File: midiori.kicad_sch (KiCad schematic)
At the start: 73 parts, among them J1 midiori-rescue_x68000_expansi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, J2 Conn_ARM_JTAG_SWD_10, J3 AudioJack3, J4 Mini-DIN-5, J5 AudioJack3, J6 AudioJack3, U1 74LCX07, U10 ICE40HX1K-VQ100, U11 AP2205K-3.3, U12 AK4432, U13 TL074, U14 AP2205K-3.3, U2 AT25SF081-SSHD-X, U3 AP2127K-1.2, U4 SN74LVC8T245DWR, U5 SN74LVC8T245DWR, U6 SN74LVC8T245DWR, U7 SN74LVC8T245DWR, U8 SN74LVC8T245DWR, U9 SN74LVC8T245DWR, X1 16MHz, X2 24.576MHz

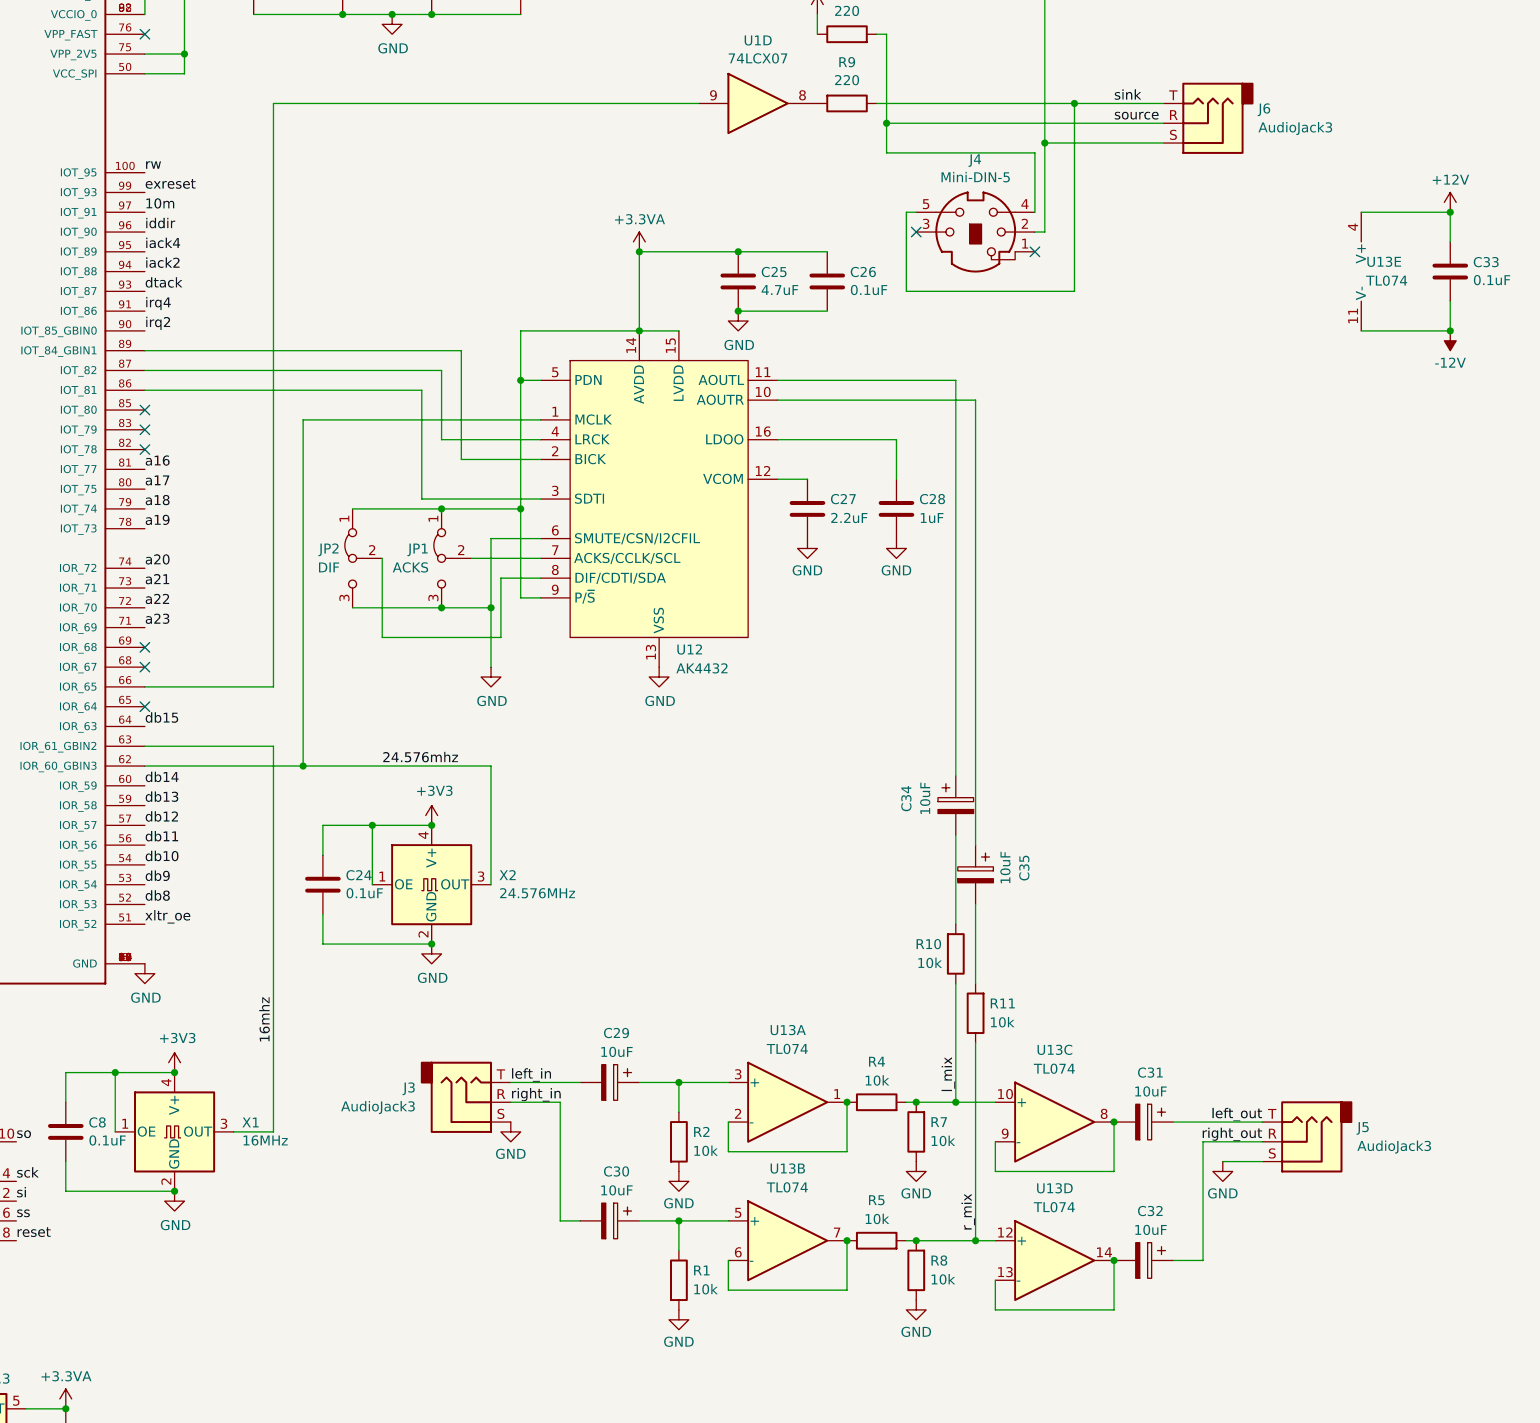
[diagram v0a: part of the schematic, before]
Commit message: small schematic changes
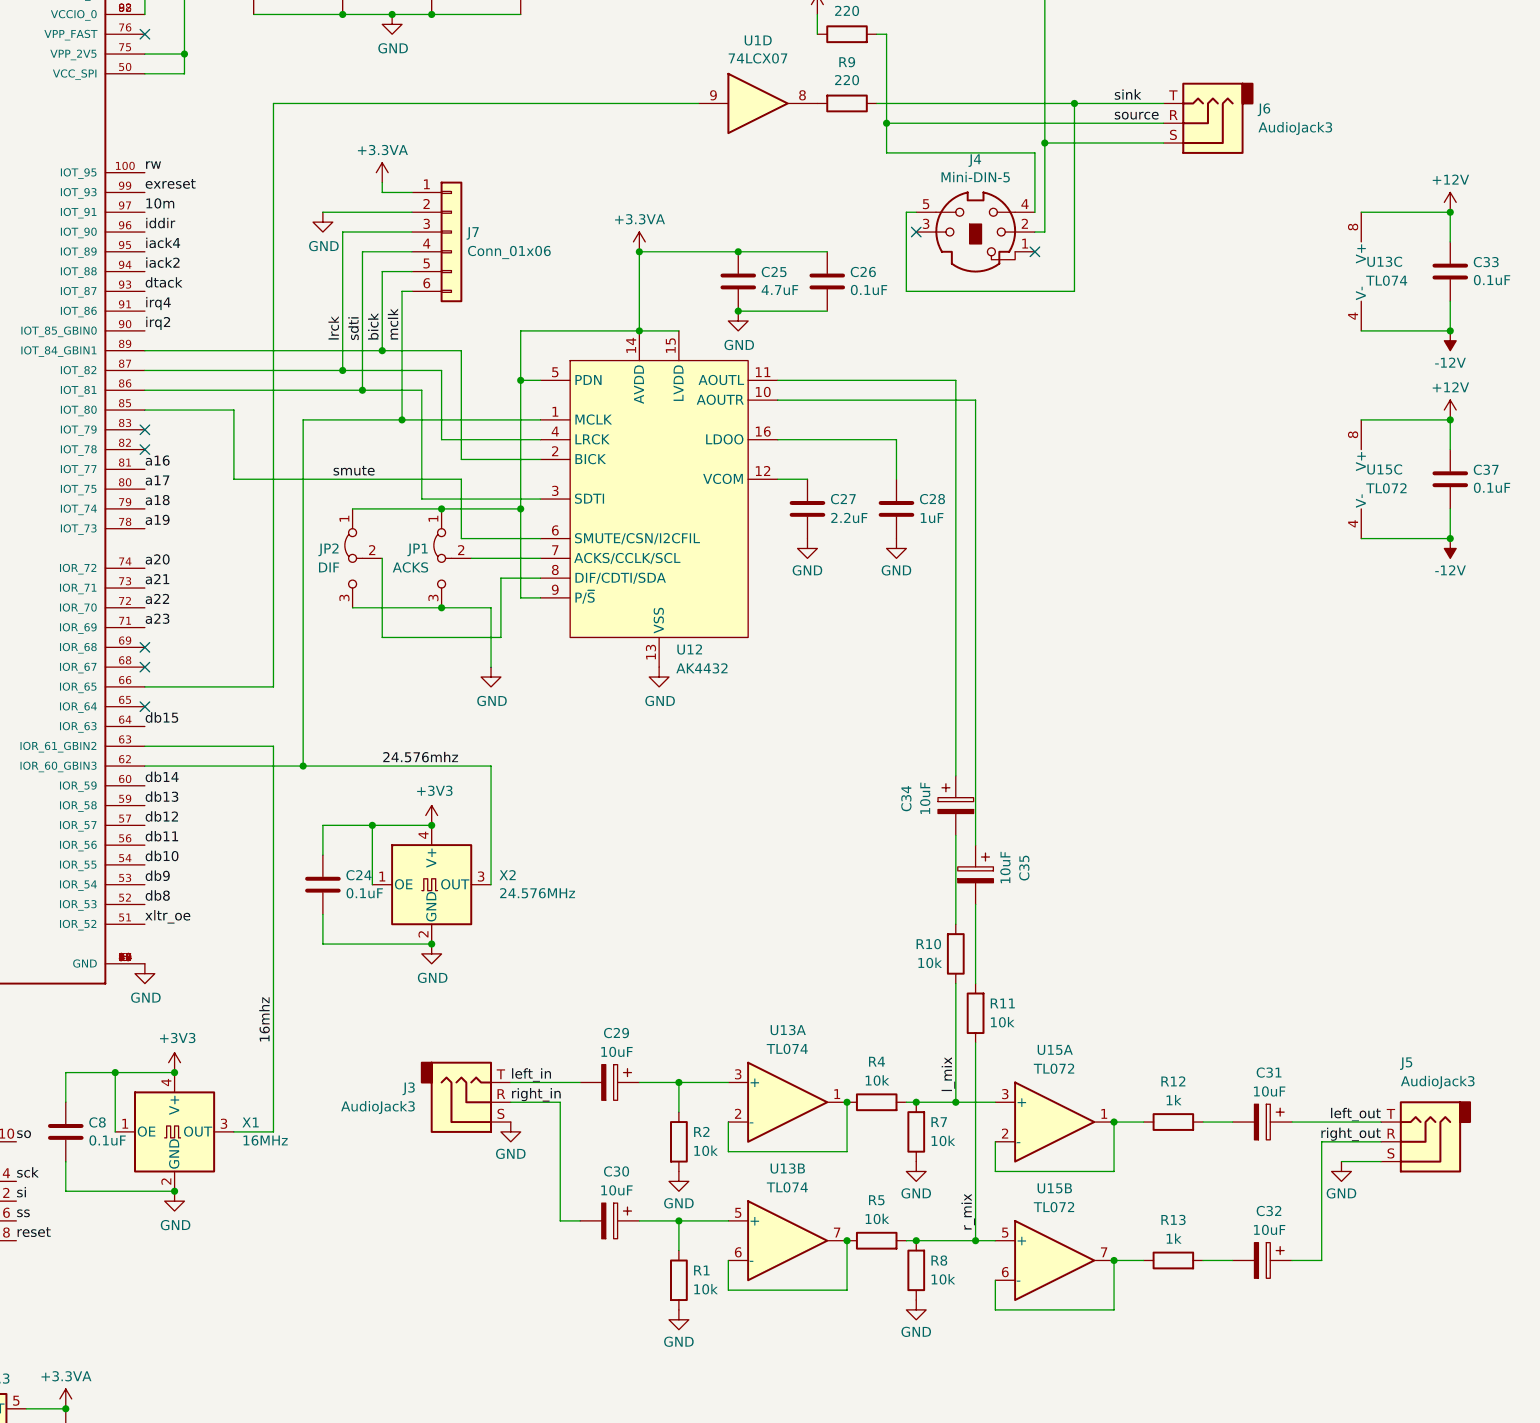
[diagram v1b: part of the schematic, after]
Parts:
- removed unit 4 of U13
- removed unit 5 of U13
- added C37: 0.1uF, Capacitor_SMD:C_0805_2012Metric, symbol Device:C
- added J7: Conn_01x06, Connector_PinHeader_2.54mm:PinHeader_1x06_P2.54mm_Vertical, symbol Connector_Generic:Conn_01x06
- added R12, R13: 1k, Resistor_SMD:R_0805_2012Metric, symbol Device:R
- added U15: TL072, Package_SO:SOIC-8_3.9x4.9mm_P1.27mm, symbol Amplifier_Operational:TL072
- C24, C8: footprint Capacitor_SMD:C_0805_2012Metric_Pad1.15x1.40mm_HandSolder -> Capacitor_SMD:C_0805_2012Metric
- C27, C28: footprint (none) -> Capacitor_SMD:C_0805_2012Metric
- C29, C30, C31, C32, C34, C35: footprint (none) -> Capacitor_SMD:C_Elec_5x5.8; Digikey (none) -> 565-HHXD350ARA220ME61GCT-ND
- J3, J5, J6: footprint (none) -> Connector_Audio:Jack_3.5mm_CUI_SJ1-3533NG_Horizontal
- R1, R10, R11, R2, R4, R5, R7, R8: footprint (none) -> Resistor_SMD:R_0805_2012Metric
- U10: Digikey (none) -> 220-1567-ND
- U12: Digikey (none) -> 974-1078-1-ND
- U13: footprint (none) -> Package_SO:SOIC-8_3.9x4.9mm_P1.27mm; symbol Amplifier_Operational:TL074 -> Amplifier_Operational:TL072
- U4, U5, U6, U7, U8, U9: Digikey (none) -> 1727-8095-1-ND
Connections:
- net +12V: now also U13.8 (V+), C37.1, U15.8 (V+)
- net +3.3VA: now also J7.1 (Pin_1)
- net -12V: now also U13.4 (V-), C37.2, U15.4 (V-)
- net 24.576mhz: now also J7.6 (Pin_6)
- net GND: now also J7.2 (Pin_2); no longer U12.6 (SMUTE/CSN/I2CFIL)
- net l_mix: now also U15.3 (+); no longer U13.10 (+)
- net r_mix: now also U15.5 (+)
- net smute: now reaches U10.85 (IOT_80)
- net smute: now also U12.6 (SMUTE/CSN/I2CFIL)
- net sdti: now reaches U10.86 (IOT_81), U12.3 (SDTI)
- net sdti: now also J7.4 (Pin_4)
- net lrck: now reaches U10.87 (IOT_82), U12.4 (LRCK)
- net lrck: now also J7.3 (Pin_3)
- net bick: now reaches U10.89 (IOT_84_GBIN1), U12.2 (BICK)
- net bick: now also J7.5 (Pin_5)
- net at C32.2: now also R13.2
- new net: R12.1, U15.1, U15.2 (-)
- new net: C31.2, R12.2
- new net: R13.1, U15.6 (-), U15.7
- no-connect marks 50 -> 49
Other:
- moved on the sheet: C31, C32, J5

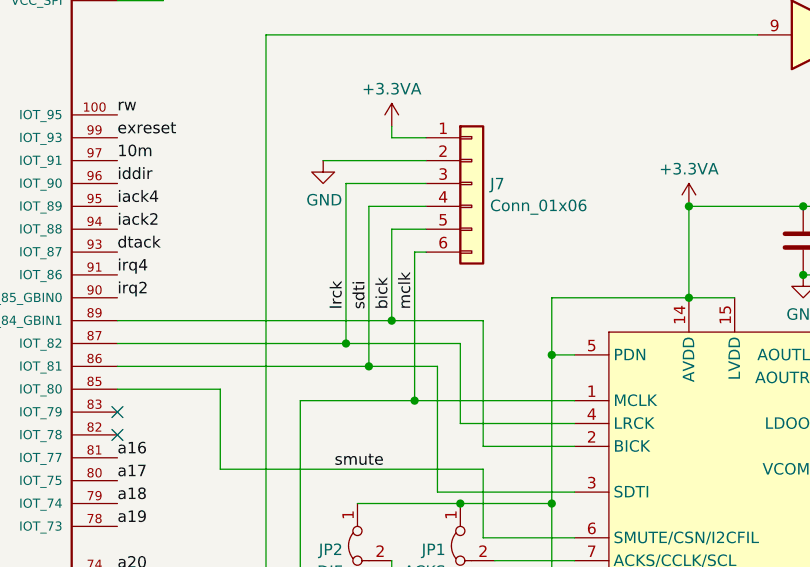
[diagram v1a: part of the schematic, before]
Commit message: convert pcb version
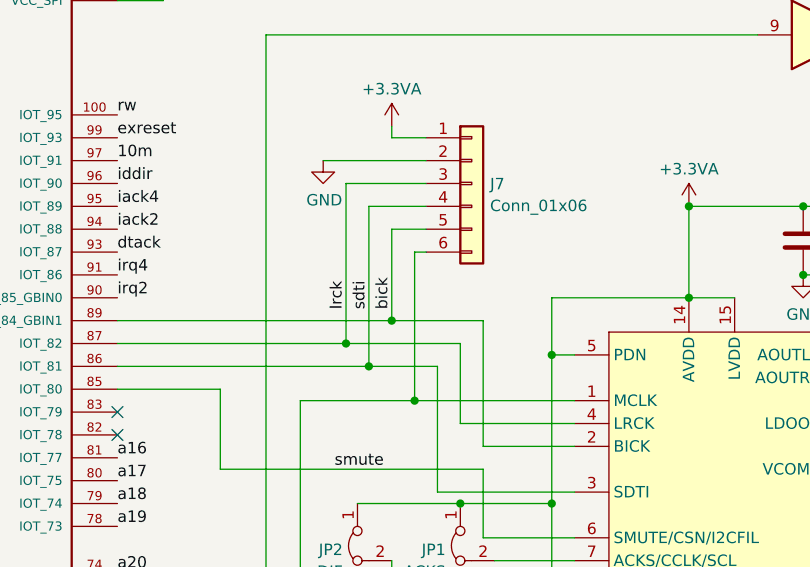
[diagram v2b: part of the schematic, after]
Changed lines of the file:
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@@
-		)
-	)
-	(label "mclk"
-		(at 278.13 102.87 90)
-		(fields_autoplaced yes)
-		(effects
-			(font
-				(size 1.27 1.27)
-			)
-			(justify left bottom)
 		)
 	)

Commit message: switch to single psu translator
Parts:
- added R14: R, symbol Device:R
- U4, U5, U6, U7, U8, U9: value SN74LVC8T245DWR -> SN74LVC245APW; footprint SOIC127P1030X265-24N -> Package_SO:TSSOP-20_4.4x6.5mm_P0.65mm; symbol midiori-rescue:SN74LVC8T245DWR-SN74LVC8T245DWR-midiori-rescue-midiori-rescue -> Logic_LevelTranslator:SN74LVC245APW
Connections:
- net +3V3: now also U4.20 (VCC), U5.20 (VCC), U6.20 (VCC), U7.20 (VCC), U8.1 (DIR), U8.20 (VCC), U9.20 (VCC), R14.1; no longer U4.23 (VCCB), U4.24 (VCCB), U5.23 (VCCB), U5.24 (VCCB), U6.23 (VCCB), U6.24 (VCCB), U7.23 (VCCB), U7.24 (VCCB), U8.23 (VCCB), U8.24 (VCCB), U9.23 (VCCB), U9.24 (VCCB)
- net +5V: no longer U4.1 (VCCA), U4.2 (DIR), U5.1 (VCCA), U5.2 (DIR), U6.1 (VCCA), U6.2 (DIR), U7.1 (VCCA), U8.1 (VCCA), U8.2 (DIR), U9.1 (VCCA)
- net 10MHz: now also U8.2 (A1); no longer U8.3 (A1)
- net 10m: now also U8.18 (B1); no longer U8.21 (B1)
- net AB1: now also U4.9 (A8); no longer U4.10 (A8)
- net AB10: now also U5.7 (A6); no longer U5.8 (A6)
- net AB11: now also U5.6 (A5); no longer U5.7 (A5)
- net AB12: now also U5.5 (A4); no longer U5.6 (A4)
- net AB13: now also U5.4 (A3); no longer U5.5 (A3)
- net AB14: now also U5.3 (A2); no longer U5.4 (A2)
- net AB15: now also U5.2 (A1); no longer U5.3 (A1)
- net AB16: now also U6.9 (A8); no longer U6.10 (A8)
- net AB17: now also U6.8 (A7); no longer U6.9 (A7)
- net AB18: now also U6.7 (A6); no longer U6.8 (A6)
- net AB19: now also U6.6 (A5); no longer U6.7 (A5)
- net AB2: now also U4.8 (A7); no longer U4.9 (A7)
- net AB20: now also U6.5 (A4); no longer U6.6 (A4)
- net AB21: now also U6.4 (A3); no longer U6.5 (A3)
- net AB22: now also U6.3 (A2); no longer U6.4 (A2)
- net AB23: now also U6.2 (A1); no longer U6.3 (A1)
- net AB3: now also U4.7 (A6); no longer U4.8 (A6)
- net AB4: now also U4.6 (A5); no longer U4.7 (A5)
- net AB5: now also U4.5 (A4); no longer U4.6 (A4)
- net AB6: now also U4.4 (A3); no longer U4.5 (A3)
- net AB7: now also U4.3 (A2); no longer U4.4 (A2)
- net AB8: now also U5.9 (A8); no longer U5.10 (A8)
- net AB9: now also U5.8 (A7); no longer U5.9 (A7)
- net AS: now also U8.6 (A5); no longer U8.7 (A5)
- net DB0: now also U7.9 (A8); no longer U7.10 (A8)
- net DB1: now also U7.8 (A7); no longer U7.9 (A7)
- net DB10: now also U9.7 (A6); no longer U9.8 (A6)
- net DB11: now also U9.6 (A5); no longer U9.7 (A5)
- net DB12: now also U9.5 (A4); no longer U9.6 (A4)
- net DB13: now also U9.4 (A3); no longer U9.5 (A3)
- net DB14: now also U9.3 (A2); no longer U9.4 (A2)
- net DB15: now also U9.2 (A1); no longer U9.3 (A1)
- net DB2: now also U7.7 (A6); no longer U7.8 (A6)
- net DB3: now also U7.6 (A5); no longer U7.7 (A5)
- net DB4: now also U7.5 (A4); no longer U7.6 (A4)
- net DB5: now also U7.4 (A3); no longer U7.5 (A3)
- net DB6: now also U7.3 (A2); no longer U7.4 (A2)
- net DB7: now also U7.2 (A1); no longer U7.3 (A1)
- net DB8: now also U9.9 (A8); no longer U9.10 (A8)
- net DB9: now also U9.8 (A7); no longer U9.9 (A7)
- net EXRESET: now also U8.3 (A2); no longer U8.4 (A2)
- net GND: now also U4.10 (GND), U4.18 (B1), U4.19 (~{OE}), U4.2 (A1), U5.10 (GND), U5.19 (~{OE}), U6.10 (GND), U6.19 (~{OE}), U7.10 (GND), U8.10 (GND), U8.19 (~{OE}), U9.10 (GND); no longer U4.11 (GND), U4.12 (GND), U4.13 (GND), U4.21 (B1), U4.22 (OE), U4.3 (A1), U5.11 (GND), U5.12 (GND), U5.13 (GND), U5.22 (OE), U6.11 (GND), U6.12 (GND), U6.13 (GND), U6.22 (OE), U7.11 (GND), U7.12 (GND), U7.13 (GND), U8.11 (GND), U8.12 (GND), U8.13 (GND), U8.22 (OE), U9.11 (GND), U9.12 (GND), U9.13 (GND)
- net IACK2: now also U8.7 (A6); no longer U8.8 (A6)
- net IACK4: now also U8.8 (A7); no longer U8.9 (A7)
- net IDDIR: now also U7.1 (DIR), U8.9 (A8), U9.1 (DIR); no longer U7.2 (DIR), U8.10 (A8), U9.2 (DIR)
- net LDS: now also U8.5 (A4); no longer U8.6 (A4)
- net RW: now also U8.4 (A3); no longer U8.5 (A3)
- net a1: now also U4.11 (B8); no longer U4.14 (B8)
- net a16: now also U6.11 (B8); no longer U6.14 (B8)
- net a17: now also U6.12 (B7); no longer U6.15 (B7)
- net a18: now also U6.13 (B6); no longer U6.16 (B6)
- net a19: now also U6.14 (B5); no longer U6.17 (B5)
- net a2: now also U4.12 (B7); no longer U4.15 (B7)
- net a20: now also U6.15 (B4); no longer U6.18 (B4)
- net a21: now also U6.16 (B3); no longer U6.19 (B3)
- net a22: now also U6.17 (B2); no longer U6.20 (B2)
- net a23: now also U6.18 (B1); no longer U6.21 (B1)
- net a3: now also U4.13 (B6); no longer U4.16 (B6)
- net a4: now also U4.14 (B5); no longer U4.17 (B5)
- net a5: now also U4.15 (B4); no longer U4.18 (B4)
- net a6: now also U4.16 (B3); no longer U4.19 (B3)
- net a7: now also U4.17 (B2); no longer U4.20 (B2)
- net ab10: now also U5.13 (B6); no longer U5.16 (B6)
- net ab11: now also U5.14 (B5); no longer U5.17 (B5)
- net ab12: now also U5.15 (B4); no longer U5.18 (B4)
- net ab13: now also U5.16 (B3); no longer U5.19 (B3)
- net ab14: now also U5.17 (B2); no longer U5.20 (B2)
- net ab15: now also U5.18 (B1); no longer U5.21 (B1)
- net ab8: now also U5.11 (B8); no longer U5.14 (B8)
- net ab9: now also U5.12 (B7); no longer U5.15 (B7)
- net as: now also U8.14 (B5); no longer U8.17 (B5)
- net d0: now also U7.11 (B8); no longer U7.14 (B8)
- net d1: now also U7.12 (B7); no longer U7.15 (B7)
- net d2: now also U7.13 (B6); no longer U7.16 (B6)
- net d3: now also U7.14 (B5); no longer U7.17 (B5)
- net d4: now also U7.15 (B4); no longer U7.18 (B4)
- net d5: now also U7.16 (B3); no longer U7.19 (B3)
- net d6: now also U7.17 (B2); no longer U7.20 (B2)
- net d7: now also U7.18 (B1); no longer U7.21 (B1)
- net db10: now also U9.13 (B6); no longer U9.16 (B6)
- net db11: now also U9.14 (B5); no longer U9.17 (B5)
- net db12: now also U9.15 (B4); no longer U9.18 (B4)
- net db13: now also U9.16 (B3); no longer U9.19 (B3)
- net db14: now also U9.17 (B2); no longer U9.20 (B2)
- net db15: now also U9.18 (B1); no longer U9.21 (B1)
- net db8: now also U9.11 (B8); no longer U9.14 (B8)
- net db9: now also U9.12 (B7); no longer U9.15 (B7)
- net exreset: now also U8.17 (B2); no longer U8.20 (B2)
- net iack2: now also U8.13 (B6); no longer U8.16 (B6)
- net iack4: now also U8.12 (B7); no longer U8.15 (B7)
- net iddir: now also U8.11 (B8); no longer U8.14 (B8)
- net lds: now also U8.15 (B4); no longer U8.18 (B4)
- net rw: now also U8.16 (B3); no longer U8.19 (B3)
- net xltr_oe: now also U7.19 (~{OE}), U9.19 (~{OE}); no longer U7.22 (OE), U9.22 (OE)
- net addr_dir: now reaches U10.69 (IOR_68)
- net addr_dir: now also U4.1 (DIR), U5.1 (DIR), U6.1 (DIR), R14.2
- no-connect marks 49 -> 48

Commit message: add bus mastering and midi in
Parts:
- removed unit 6 of U1
- added J8: AudioJack3, Connector_Audio:Jack_3.5mm_CUI_SJ1-3533NG_Horizontal, symbol Connector_Audio:AudioJack3
- added J9: Mini-DIN-5, x68k:MD-50SM, symbol Connector:Mini-DIN-5
- added R15, R16: 220, symbol Device:R
- added U16: 74LCX07, Package_SO:SOIC-14_3.9x8.7mm_P1.27mm, symbol 74xx:74LCX07
- added U17: PC817, Package_DIP:DIP-4_W7.62mm, symbol Isolator:PC817
- added U18: SN74LVC245APW, Package_SO:SOIC-20W_7.5x12.8mm_P1.27mm, symbol Logic_LevelTranslator:SN74LVC245APW
- U1: footprint (none) -> Package_SO:SOIC-14_3.9x8.7mm_P1.27mm
- U4, U5, U6, U7, U8, U9: footprint Package_SO:TSSOP-20_4.4x6.5mm_P0.65mm -> Package_SO:SOIC-20W_7.5x12.8mm_P1.27mm
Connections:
- net +3V3: now also R16.2, U16.14 (VCC), U18.20 (VCC); no longer U8.1 (DIR)
- net AS: now also U16.6
- net GND: now also U8.1 (DIR), J8.S, J9.2, U16.7 (GND), U17.3, U18.1 (DIR), U18.10 (GND), U18.19 (~{OE}); no longer U1.11
- net IDDIR: no longer U7.1 (DIR), U8.9 (A8), U9.1 (DIR)
- net LDS: now also U16.12
- net bg: now reaches U10.3 (IOL_2A)
- net bg: now also U18.2 (A1)
- net midi_in: now reaches U10.4 (IOL_2B)
- net midi_in: now also R16.1, U17.4
- net rw_drv: now reaches U10.41 (IOB_42_CBSEL0)
- net as_drv: now reaches U10.42 (IOB_43_CBSEL1)
- net as_drv: now also U16.5
- net bgack: now reaches U10.65 (IOR_64)
- net bgack: now also U16.11
- net midi_out: now reaches U1.9, U10.66 (IOR_65)
- net br: now reaches U10.68 (IOR_67)
- net br: now also U1.11
- net uds_lds_drv: now reaches U10.7 (IOL_3A)
- net uds_lds_drv: now also U16.13, U16.9
- net exown: now reaches U10.82 (IOT_78)
- net exown: now also U16.1
- net uds: now reaches U10.83 (IOT_79)
- net uds: now also U18.3 (A2)
- net BR: now reaches U1.10
- net iddir: no longer names the net of U8.11 (B8)
- net iddir: no longer U10.96 (IOT_90)
- new net: R15.1, U17.1
- new net: J8.T, J9.5, R15.2
- new net: J8.R, J9.4, U17.2
- new net BG: U18.18 (B1)
- new net BGACK: U16.10
- new net EXOWN: U16.2
- new net EXREQ: U16.4
- new net UDS: U16.8, U18.17 (B2)
- new net data_dir: U10.96 (IOT_90), U7.1 (DIR), U9.1 (DIR)
- new net exreq: U16.3
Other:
- moved on the sheet: U1A, U1B, U1C, U1E, U1G
